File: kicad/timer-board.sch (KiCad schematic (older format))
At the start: 16 parts, among them J1 Conn_PWR, J2 Conn_Data, SW1 SW_SPST, SW2 SW_SPDT, U1 NE555DR, U2 SN74HC00DR

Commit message: More work
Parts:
- added D2: LED - red FV 2V, LED_SMD:LED_0603_1608Metric, symbol Device:LED
- added R6: 150, Resistor_SMD:R_0201_0603Metric, symbol Device:R
- D1: JLCPCD Part (none) -> 19-217/BHC-ZL1M2RY/3T
- R4: value 100K -> 1K
- R5: PLCPCB Part (none) -> 0603WAF1200T5E
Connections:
- net +5V: no longer R4.1, U2.5 (2B)
- net GND: now also R4.2, R6.2; no longer U2.10 (3B), U2.9 (3A)
- net at D1.2 (A), U2.6 (2Y): now also J2.1 (Pin_1)
- net at U2.3 (1Y), U2.4 (2A): now also U2.5 (2B); no longer J2.1 (Pin_1)
- net ~Hold~: now reaches U2.8 (3Y)
- net ~Hold~: now also U2.2 (1B)
- new net: D2.2 (A), J2.2 (Pin_2)
- new net: D2.1 (K), R6.1
- new net Hold: R4.1, U2.10 (3B), U2.9 (3A)
- no-connect marks 4 -> 3
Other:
- moved on the sheet: J2

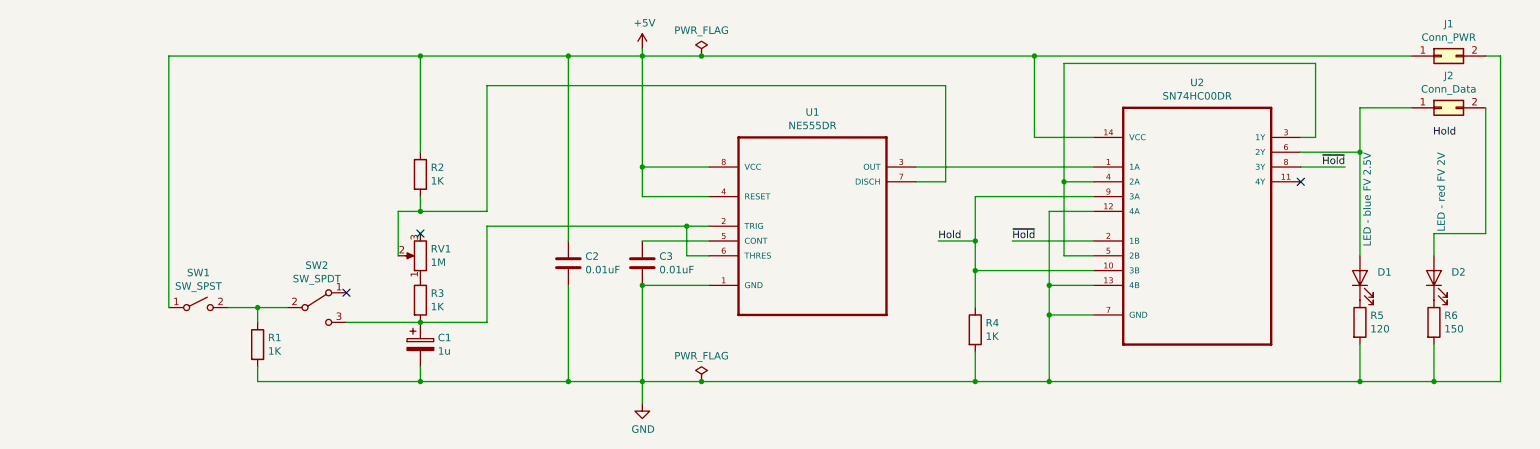
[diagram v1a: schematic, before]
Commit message: Thicken VCC
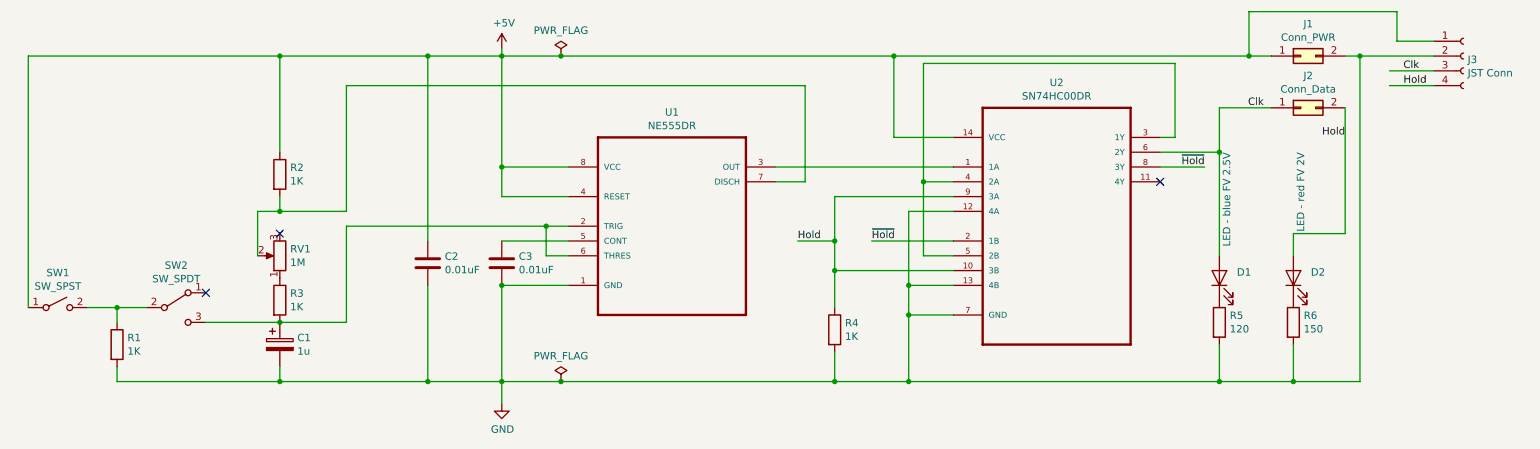
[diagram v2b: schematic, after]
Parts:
- added J3: JST Conn, Connector_JST:JST_XH_B4B-XH-AM_1x04_P2.50mm_Vertical, symbol Connector:Conn_01x04_Female
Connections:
- net +5V: now also J3.1 (Pin_1)
- net GND: now also J3.2 (Pin_2)
- net Hold: now also D2.2 (A), J2.2 (Pin_2), J3.4 (Pin_4)
- net Clk: now reaches D1.2 (A), J2.1 (Pin_1), U2.6 (2Y)
- net Clk: now also J3.3 (Pin_3)
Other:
- moved on the sheet: C1, C2, C3, D1, D2, J1, J2, R1, R2, R3, R4, R5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

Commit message: Add bill of materials etc
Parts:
- C1: LCSC (none) -> C15849
- C2, C3: LCSC (none) -> C57112
- D1: JLCPCB Part (none) -> 19-217/BHC-ZL1M2RY/3T; JLCPCD Part 19-217/BHC-ZL1M2RY/3T -> (none); LCSC (none) -> C72041
- D2: LCSC (none) -> C2286
- R1, R2, R3, R4: LCSC (none) -> C21190
- R5: JLCPCB Part (none) -> 0603WAF1200T5E; LCSC (none) -> C22787; PLCPCB Part 0603WAF1200T5E -> (none)
- R6: JLCPCB Part (none) -> 0603WAF1500T5E; LCSC (none) -> C22808; PLCPCB Part 0603WAF1500T5E -> (none)
- U1: LCSC (none) -> C7593
- U2: LCSC (none) -> C10090
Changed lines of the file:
@@
 F 7 "None" H 5200 3050 50  0001 L BNN "Field7"
 F 8 "Peripheral circuit; astable/monostable, timer; 500kHz;" H 5200 3050 50  0001 L BNN "Field8"
+F 9 "C7593" H 5200 3050 50  0001 C CNN "LCSC"
 	1    5200 3050
 	1    0    0    -1
@@
 F 2 "Capacitor_SMD:C_0201_0603Metric" H 4088 3250 50  0001 C CNN
 F 3 "~" H 4050 3400 50  0001 C CNN
+F 4 "C57112" H 4050 3400 50  0001 C CNN "LCSC"
 	1    4050 3400
 	1    0    0    -1
@@
 F 2 "Capacitor_SMD:C_0201_0603Metric" H 2588 3800 50  0001 C CNN
 F 3 "~" H 2550 3950 50  0001 C CNN
+F 4 "C15849" H 2550 3950 50  0001 C CNN "LCSC"
 	1    2550 3950
 	1    0    0    -1
@@
 F 2 "Resistor_SMD:R_0201_0603Metric" V 2480 3650 50  0001 C CNN
 F 3 "~" H 2550 3650 50  0001 C CNN
+F 4 "C21190" H 2550 3650 50  0001 C CNN "LCSC"
 	1    2550 3650
 	1    0    0    -1
@@
 F 2 "Resistor_SMD:R_0201_0603Metric" V 2480 2800 50  0001 C CNN
 F 3 "~" H 2550 2800 50  0001 C CNN
+F 4 "C21190" H 2550 2800 50  0001 C CNN "LCSC"
 	1    2550 2800
 	1    0    0    -1
@@
 F 2 "Capacitor_SMD:C_0201_0603Metric" H 3588 3250 50  0001 C CNN
 F 3 "~" H 3550 3400 50  0001 C CNN
+F 4 "C57112" H 3550 3400 50  0001 C CNN "LCSC"
 	1    3550 3400
 	1    0    0    -1
@@
 F 2 "LED_SMD:LED_0603_1608Metric" H 8900 3500 50  0001 C CNN
 F 3 "https://datasheet.lcsc.com/szlcsc/Everlight-Elec-19-217-BHC-ZL1M2RY-3T_C72041.pdf" H 8900 3500 50  0001 C CNN
-F 4 "19-217/BHC-ZL1M2RY/3T" V 8900 3500 50  0001 C CNN "JLCPCD Part"
+F 4 "19-217/BHC-ZL1M2RY/3T" V 8900 3500 50  0001 C CNN "JLCPCB Part"
+F 5 "C72041" H 8900 3500 50  0001 C CNN "LCSC"
 	1    8900 3500
 	0    -1   -1   0
@@
 F 2 "Resistor_SMD:R_0201_0603Metric" V 8830 3800 50  0001 C CNN
 F 3 "~" H 8900 3800 50  0001 C CNN
-F 4 "0603WAF1200T5E" H 8900 3800 50  0001 C CNN "PLCPCB Part"
+F 4 "0603WAF1200T5E" H 8900 3800 50  0001 C CNN "JLCPCB Part"
+F 5 "C22787" H 8900 3800 50  0001 C CNN "LCSC"
 	1    8900 3800
 	1    0    0    -1
@@
 F 2 "Resistor_SMD:R_0201_0603Metric" V 1380 3950 50  0001 C CNN
 F 3 "~" H 1450 3950 50  0001 C CNN
+F 4 "C21190" H 1450 3950 50  0001 C CNN "LCSC"
 	1    1450 3950
 	1    0    0    -1
@@
 F 7 "IC: digital; inverter; NAND; Channels: 4; Inputs: 2; SMD;" H 7800 3050 50  0001 L BNN "Field7"
 F 8 "https://www.digikey.com/product-detail/en/texas-instruments/SN74HC00DR/296-1187-1-ND/404900?utm_source=snapeda&utm_medium=aggregator&utm_campaign=symbol" H 7800 3050 50  0001 L BNN "Field8"
+F 9 "C10090" H 7800 3050 50  0001 C CNN "LCSC"
 	1    7800 3050
 	1    0    0    -1
@@
 F 2 "Resistor_SMD:R_0201_0603Metric" V 6230 3850 50  0001 C CNN
 F 3 "~" H 6300 3850 50  0001 C CNN
+F 4 "C21190" H 6300 3850 50  0001 C CNN "LCSC"
 	1    6300 3850
 	1    0    0    -1
@@
 F 3 "https://datasheet.lcsc.com/szlcsc/Hubei-KENTO-Elec-KT-0603R_C2286.pdf" H 9400 3500 50  0001 C CNN
 F 4 "KT-0603R" V 9400 3500 50  0001 C CNN "JLCPCB Part"
+F 5 "C2286" H 9400 3500 50  0001 C CNN "LCSC"
 	1    9400 3500
 	0    -1   -1   0
@@
 F 2 "Resistor_SMD:R_0201_0603Metric" V 9330 3800 50  0001 C CNN
 F 3 "~" H 9400 3800 50  0001 C CNN
-F 4 "0603WAF1500T5E" H 9400 3800 50  0001 C CNN "PLCPCB Part"
+F 4 "0603WAF1500T5E" H 9400 3800 50  0001 C CNN "JLCPCB Part"
+F 5 "C22808" H 9400 3800 50  0001 C CNN "LCSC"
 	1    9400 3800
 	1    0    0    -1

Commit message: Version 1.1
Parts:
- C1, C2, C3: footprint Capacitor_SMD:C_0201_0603Metric -> Capacitor_SMD:C_0603_1608Metric
- D1: JLCPCB Part 19-217/BHC-ZL1M2RY/3T -> (none)
- D2: JLCPCB Part KT-0603R -> (none)
- R1, R2, R3, R4: footprint Resistor_SMD:R_0201_0603Metric -> Resistor_SMD:R_0603_1608Metric
- R5: footprint Resistor_SMD:R_0201_0603Metric -> Resistor_SMD:R_0603_1608Metric; JLCPCB Part 0603WAF1200T5E -> (none)
- R6: footprint Resistor_SMD:R_0201_0603Metric -> Resistor_SMD:R_0603_1608Metric; JLCPCB Part 0603WAF1500T5E -> (none)
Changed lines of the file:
@@
 F 0 "C3" H 4165 3446 50  0000 L CNN
 F 1 "0.01uF" H 4165 3355 50  0000 L CNN
-F 2 "Capacitor_SMD:C_0201_0603Metric" H 4088 3250 50  0001 C CNN
+F 2 "Capacitor_SMD:C_0603_1608Metric" H 4088 3250 50  0001 C CNN
 F 3 "~" H 4050 3400 50  0001 C CNN
 F 4 "C57112" H 4050 3400 50  0001 C CNN "LCSC"
@@
 F 0 "C1" H 2668 3996 50  0000 L CNN
 F 1 "1u" H 2668 3905 50  0000 L CNN
-F 2 "Capacitor_SMD:C_0201_0603Metric" H 2588 3800 50  0001 C CNN
+F 2 "Capacitor_SMD:C_0603_1608Metric" H 2588 3800 50  0001 C CNN
 F 3 "~" H 2550 3950 50  0001 C CNN
 F 4 "C15849" H 2550 3950 50  0001 C CNN "LCSC"
@@
 F 0 "R3" H 2620 3696 50  0000 L CNN
 F 1 "1K" H 2620 3605 50  0000 L CNN
-F 2 "Resistor_SMD:R_0201_0603Metric" V 2480 3650 50  0001 C CNN
+F 2 "Resistor_SMD:R_0603_1608Metric" V 2480 3650 50  0001 C CNN
 F 3 "~" H 2550 3650 50  0001 C CNN
 F 4 "C21190" H 2550 3650 50  0001 C CNN "LCSC"
@@
 F 0 "R2" H 2620 2846 50  0000 L CNN
 F 1 "1K" H 2620 2755 50  0000 L CNN
-F 2 "Resistor_SMD:R_0201_0603Metric" V 2480 2800 50  0001 C CNN
+F 2 "Resistor_SMD:R_0603_1608Metric" V 2480 2800 50  0001 C CNN
 F 3 "~" H 2550 2800 50  0001 C CNN
 F 4 "C21190" H 2550 2800 50  0001 C CNN "LCSC"
@@
 F 0 "C2" H 3665 3446 50  0000 L CNN
 F 1 "0.01uF" H 3665 3355 50  0000 L CNN
-F 2 "Capacitor_SMD:C_0201_0603Metric" H 3588 3250 50  0001 C CNN
+F 2 "Capacitor_SMD:C_0603_1608Metric" H 3588 3250 50  0001 C CNN
 F 3 "~" H 3550 3400 50  0001 C CNN
 F 4 "C57112" H 3550 3400 50  0001 C CNN "LCSC"
@@
 F 2 "LED_SMD:LED_0603_1608Metric" H 8900 3500 50  0001 C CNN
 F 3 "https://datasheet.lcsc.com/szlcsc/Everlight-Elec-19-217-BHC-ZL1M2RY-3T_C72041.pdf" H 8900 3500 50  0001 C CNN
-F 4 "19-217/BHC-ZL1M2RY/3T" V 8900 3500 50  0001 C CNN "JLCPCB Part"
-F 5 "C72041" H 8900 3500 50  0001 C CNN "LCSC"
+F 4 "C72041" H 8900 3500 50  0001 C CNN "LCSC"
 	1    8900 3500
 	0    -1   -1   0
@@
 F 0 "R5" H 8970 3846 50  0000 L CNN
 F 1 "120" H 8970 3755 50  0000 L CNN
-F 2 "Resistor_SMD:R_0201_0603Metric" V 8830 3800 50  0001 C CNN
+F 2 "Resistor_SMD:R_0603_1608Metric" V 8830 3800 50  0001 C CNN
 F 3 "~" H 8900 3800 50  0001 C CNN
-F 4 "0603WAF1200T5E" H 8900 3800 50  0001 C CNN "JLCPCB Part"
-F 5 "C22787" H 8900 3800 50  0001 C CNN "LCSC"
+F 4 "C22787" H 8900 3800 50  0001 C CNN "LCSC"
 	1    8900 3800
 	1    0    0    -1
@@
 F 0 "R1" H 1520 3996 50  0000 L CNN
 F 1 "1K" H 1520 3905 50  0000 L CNN
-F 2 "Resistor_SMD:R_0201_0603Metric" V 1380 3950 50  0001 C CNN
+F 2 "Resistor_SMD:R_0603_1608Metric" V 1380 3950 50  0001 C CNN
 F 3 "~" H 1450 3950 50  0001 C CNN
 F 4 "C21190" H 1450 3950 50  0001 C CNN "LCSC"
@@
 F 0 "R4" H 6370 3896 50  0000 L CNN
 F 1 "1K" H 6370 3805 50  0000 L CNN
-F 2 "Resistor_SMD:R_0201_0603Metric" V 6230 3850 50  0001 C CNN
+F 2 "Resistor_SMD:R_0603_1608Metric" V 6230 3850 50  0001 C CNN
 F 3 "~" H 6300 3850 50  0001 C CNN
 F 4 "C21190" H 6300 3850 50  0001 C CNN "LCSC"
@@
 F 2 "LED_SMD:LED_0603_1608Metric" H 9400 3500 50  0001 C CNN
 F 3 "https://datasheet.lcsc.com/szlcsc/Hubei-KENTO-Elec-KT-0603R_C2286.pdf" H 9400 3500 50  0001 C CNN
-F 4 "KT-0603R" V 9400 3500 50  0001 C CNN "JLCPCB Part"
-F 5 "C2286" H 9400 3500 50  0001 C CNN "LCSC"
+F 4 "C2286" H 9400 3500 50  0001 C CNN "LCSC"
 	1    9400 3500
 	0    -1   -1   0
@@
 F 0 "R6" H 9470 3846 50  0000 L CNN
 F 1 "150" H 9470 3755 50  0000 L CNN
-F 2 "Resistor_SMD:R_0201_0603Metric" V 9330 3800 50  0001 C CNN
+F 2 "Resistor_SMD:R_0603_1608Metric" V 9330 3800 50  0001 C CNN
 F 3 "~" H 9400 3800 50  0001 C CNN
-F 4 "0603WAF1500T5E" H 9400 3800 50  0001 C CNN "JLCPCB Part"
-F 5 "C22808" H 9400 3800 50  0001 C CNN "LCSC"
+F 4 "C22808" H 9400 3800 50  0001 C CNN "LCSC"
 	1    9400 3800
 	1    0    0    -1

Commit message: Update pot footprint
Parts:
- RV1: footprint Potentiometer_THT:Potentiometer_ACP_CA9-H5_Horizontal -> mine:6mm_trimmer
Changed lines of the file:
@@
 F 0 "RV1" H 2480 3304 50  0000 R CNN
 F 1 "1M" H 2480 3395 50  0000 R CNN
-F 2 "Potentiometer_THT:Potentiometer_ACP_CA9-H5_Horizontal" H 2550 3350 50  0001 C CNN
+F 2 "mine:6mm_trimmer" H 2550 3350 50  0001 C CNN
 F 3 "~" H 2550 3350 50  0001 C CNN
 	1    2550 3350

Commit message: Version 1.2
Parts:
- R5: value 120 -> 150; Field5 (none) -> Aiming for 16.66mA; LCSC C22787 -> C22808
- R6: value 150 -> 180; Field5 (none) -> Aiming for 16.66mA; LCSC C22808 -> C22828
- SW1: value SW_SPST -> SW_Push_SPDT; footprint mine:snap spst switch -> mine:switch_push_spdt; symbol Switch:SW_SPST -> Switch:SW_Push_SPDT
- SW2: footprint A101SYCQ04:TE_A101SYCQ04 -> mine:switch_toggle_spdt
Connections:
- net +5V: now also SW1.2 (B); no longer SW1.1 (A)
- net at R1.1, SW2.2 (B): now also SW1.1 (A); no longer SW1.2 (B)
- no-connect marks 3 -> 4
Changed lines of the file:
@@
 P 8900 3800
 F 0 "R5" H 8970 3846 50  0000 L CNN
-F 1 "120" H 8970 3755 50  0000 L CNN
+F 1 "150" H 8970 3755 50  0000 L CNN
 F 2 "Resistor_SMD:R_0603_1608Metric" V 8830 3800 50  0001 C CNN
 F 3 "~" H 8900 3800 50  0001 C CNN
-F 4 "C22787" H 8900 3800 50  0001 C CNN "LCSC"
+F 4 "C22808" H 8900 3800 50  0001 C CNN "LCSC"
+F 5 "Aiming for 16.66mA" H 8900 3800 50  0001 C CNN "Field5"
 	1    8900 3800
 	1    0    0    -1
@@
 F 0 "SW2" H 1850 3985 50  0000 C CNN
 F 1 "SW_SPDT" H 1850 3894 50  0000 C CNN
-F 2 "A101SYCQ04:TE_A101SYCQ04" H 1850 3700 50  0001 C CNN
+F 2 "mine:switch_toggle_spdt" H 1850 3700 50  0001 C CNN
 F 3 "~" H 1850 3700 50  0001 C CNN
 	1    1850 3700
@@
 Wire Wire Line
 	2550 3800 2050 3800
-Wire Wire Line
-	850  3700 850  2000
 Wire Wire Line
 	850  2000 2550 2000
@@
 P 9400 3800
 F 0 "R6" H 9470 3846 50  0000 L CNN
-F 1 "150" H 9470 3755 50  0000 L CNN
+F 1 "180" H 9470 3755 50  0000 L CNN
 F 2 "Resistor_SMD:R_0603_1608Metric" V 9330 3800 50  0001 C CNN
 F 3 "~" H 9400 3800 50  0001 C CNN
-F 4 "C22808" H 9400 3800 50  0001 C CNN "LCSC"
+F 4 "C22828" H 9400 3800 50  0001 C CNN "LCSC"
+F 5 "Aiming for 16.66mA" H 9400 3800 50  0001 C CNN "Field5"
 	1    9400 3800
 	1    0    0    -1
@@
 	9750 3200 9400 3200
 $Comp
-L Switch:SW_SPST SW1
+L Switch:SW_Push_SPDT SW1
 U 1 1 5DAAA99A
-P 1050 3700
-F 0 "SW1" H 1050 3935 50  0000 C CNN
-F 1 "SW_SPST" H 1050 3844 50  0000 C CNN
-F 2 "mine:snap spst switch" H 1050 3700 50  0001 C CNN
-F 3 "~" H 1050 3700 50  0001 C CNN
-	1    1050 3700
+P 1050 3800
+F 0 "SW1" H 1050 4035 50  0000 C CNN
+F 1 "SW_Push_SPDT" H 1050 3944 50  0000 C CNN
+F 2 "mine:switch_push_spdt" H 1050 3800 50  0001 C CNN
+F 3 "~" H 1050 3800 50  0001 C CNN
+	1    1050 3800
 	1    0    0    -1
 $EndComp
@@
 Text Label 10250 2100 2    50   ~ 0
 Clk
+Wire Wire Line
+	850  2000 850  3800
+NoConn ~ 1250 3900
 $EndSCHEMATC
